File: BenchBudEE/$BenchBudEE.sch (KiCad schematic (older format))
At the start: 0 parts

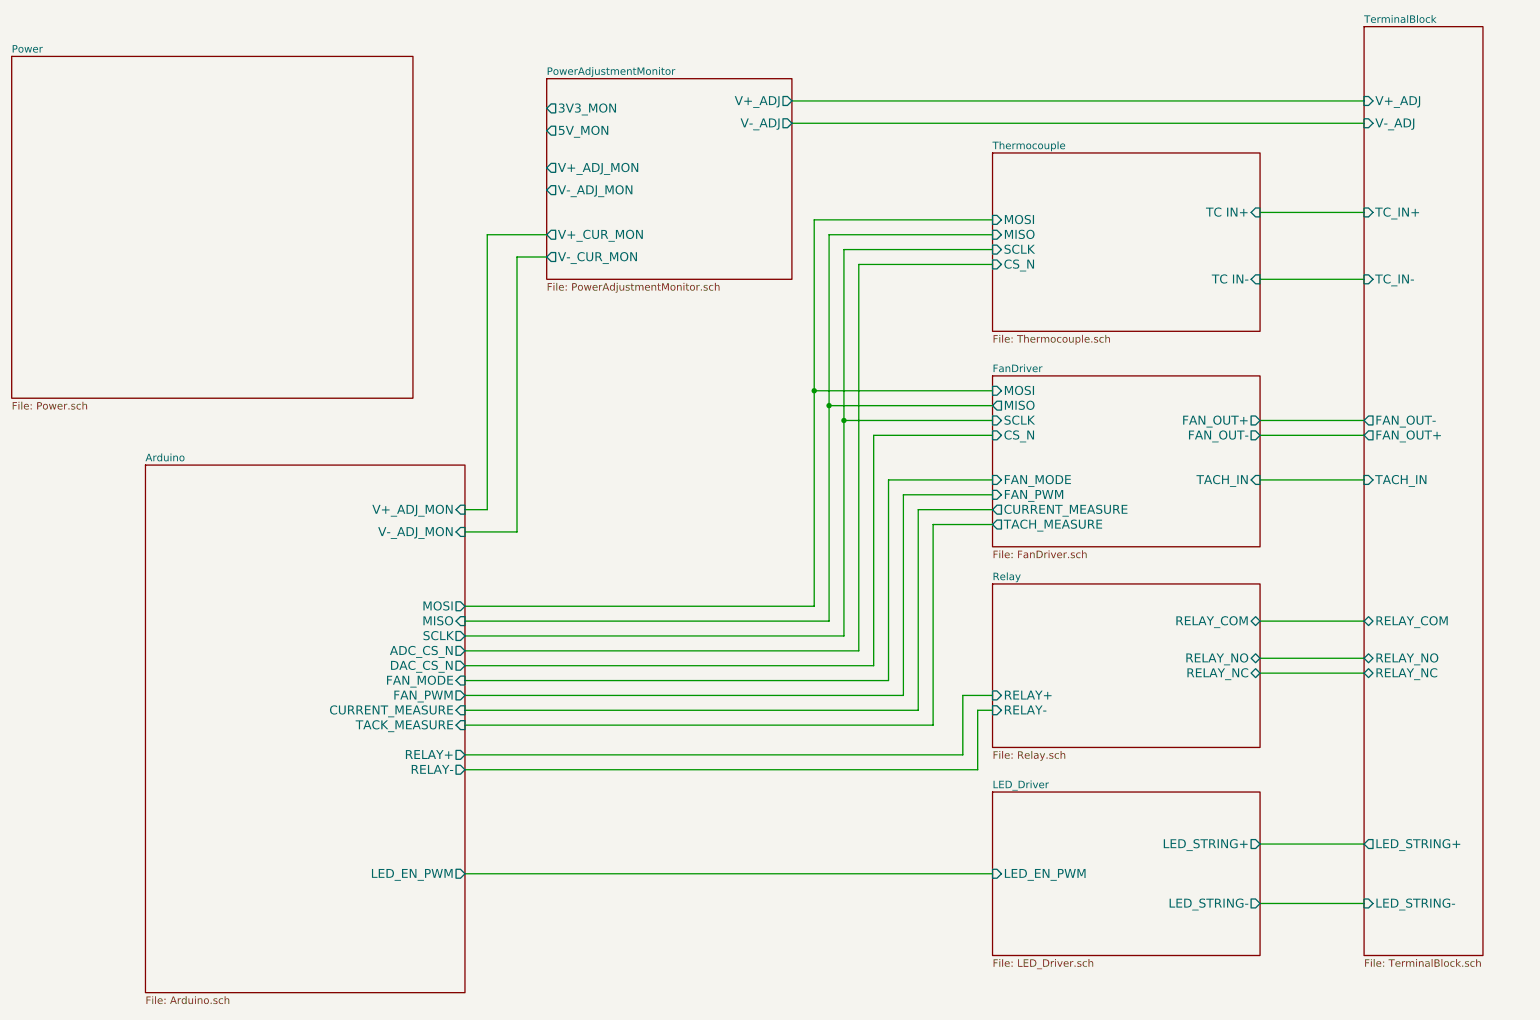
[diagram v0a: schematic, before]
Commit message: Parts added to thermocouple module. Relay & thermocouple rough placement.
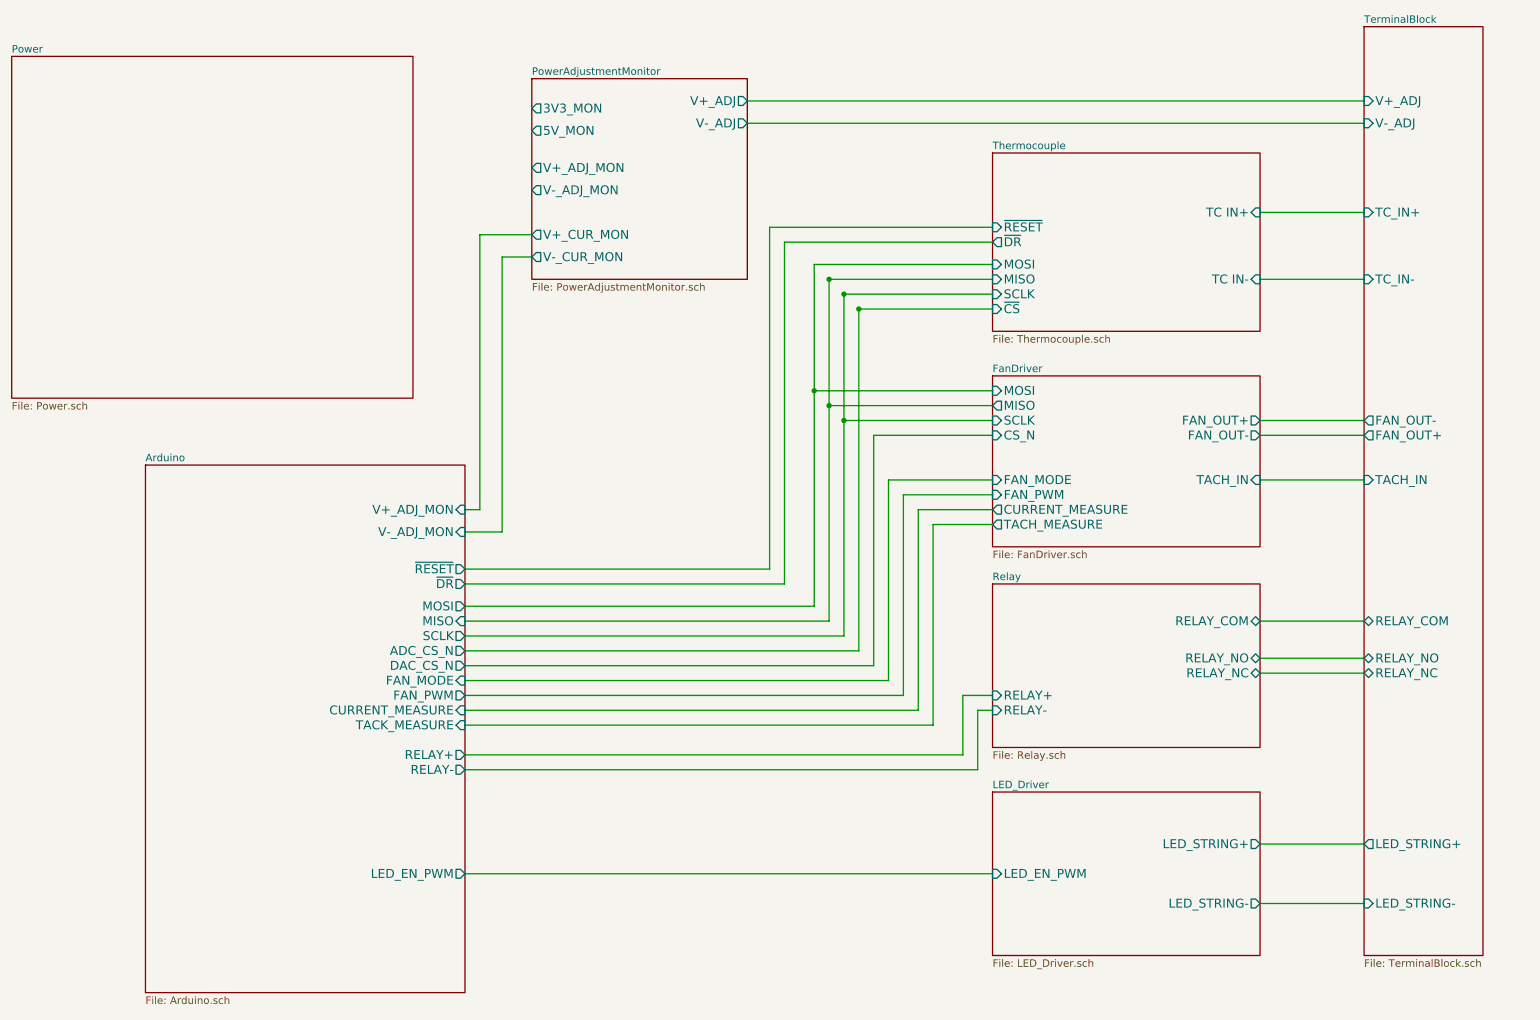
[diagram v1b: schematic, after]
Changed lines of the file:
@@
 Sheet 1 9
 Title ""
-Date "20 feb 2014"
+Date "21 feb 2014"
 Rev ""
 Comp ""
@@
 F2 "TC IN+" I R 9250 1900 60
 F3 "TC IN-" I R 9250 2350 60
-F4 "MISO" I L 7450 2050 60
-F5 "MOSI" I L 7450 1950 60
-F6 "SCLK" I L 7450 2150 60
-F7 "CS_N" I L 7450 2250 60
-$EndSheet
-$Sheet
-S 4450 1000 1650 1350
+F4 "MISO" I L 7450 2350 60
+F5 "MOSI" I L 7450 2250 60
+F6 "SCLK" I L 7450 2450 60
+F7 "~CS" I L 7450 2550 60
+F8 "~DR" O L 7450 2100 60
+F9 "~RESET" I L 7450 2000 60
+$EndSheet
+$Sheet
+S 4350 1000 1450 1350
 U 52F2C572
 F0 "PowerAdjustmentMonitor" 50
 F1 "PowerAdjustmentMonitor.sch" 50
-F2 "V+_ADJ" O R 6100 1150 60
-F3 "V-_ADJ" O R 6100 1300 60
-F4 "3V3_MON" O L 4450 1200 60
-F5 "5V_MON" O L 4450 1350 60
-F6 "V+_ADJ_MON" O L 4450 1600 60
-F7 "V-_ADJ_MON" O L 4450 1750 60
-F8 "V+_CUR_MON" O L 4450 2050 60
-F9 "V-_CUR_MON" O L 4450 2200 60
-$EndSheet
-Wire Wire Line
-	6100 1300 9950 1300
-Wire Wire Line
-	6100 1150 9950 1150
-Wire Wire Line
-	9250 3300 9950 3300
-Wire Wire Line
-	9950 3400 9250 3400
-Wire Wire Line
-	9250 3700 9950 3700
-Wire Wire Line
-	9250 2350 9950 2350
-Wire Wire Line
-	9950 1900 9250 1900
-Wire Wire Line
-	9250 5000 9950 5000
-Wire Wire Line
-	9950 4900 9250 4900
-Wire Wire Line
-	9250 4650 9950 4650
-Wire Wire Line
-	9250 6150 9950 6150
-Wire Wire Line
-	9250 6550 9950 6550
-Wire Wire Line
-	3900 3900 4050 3900
-Wire Wire Line
-	4050 3900 4050 2050
-Wire Wire Line
-	4050 2050 4450 2050
-Wire Wire Line
-	4450 2200 4250 2200
-Wire Wire Line
-	4250 2200 4250 4050
-Wire Wire Line
-	4250 4050 3900 4050
-Wire Wire Line
-	6250 1950 6250 4550
-Wire Wire Line
-	6250 1950 7450 1950
-Wire Wire Line
-	6350 2050 6350 4650
-Wire Wire Line
-	6450 2150 6450 4750
-Wire Wire Line
-	6550 2250 6550 4850
-Wire Wire Line
-	7450 3100 6250 3100
-Connection ~ 6250 3100
-Wire Wire Line
-	7450 3200 6350 3200
-Connection ~ 6350 3200
-Wire Wire Line
-	7450 3300 6450 3300
-Connection ~ 6450 3300
-Wire Wire Line
-	6950 5250 6950 3900
-Wire Wire Line
-	6950 3900 7450 3900
-Wire Wire Line
-	7450 4000 7050 4000
-Wire Wire Line
-	7050 4000 7050 5350
-Wire Wire Line
-	7450 3400 6650 3400
-Wire Wire Line
-	6650 3400 6650 4950
-Wire Wire Line
-	6550 4850 3900 4850
-Wire Wire Line
-	6650 4950 3900 4950
-Wire Wire Line
-	6250 4550 3900 4550
-Wire Wire Line
-	7450 2050 6350 2050
-Wire Wire Line
-	6450 2150 7450 2150
-Wire Wire Line
-	7450 2250 6550 2250
-Wire Wire Line
-	6350 4650 3900 4650
-Wire Wire Line
-	6450 4750 3900 4750
-Wire Wire Line
-	7450 3800 6850 3800
-Wire Wire Line
-	6850 3800 6850 5150
-Wire Wire Line
-	6850 5150 3900 5150
-Wire Wire Line
-	6950 5250 3900 5250
-Wire Wire Line
-	7050 5350 3900 5350
+F2 "V+_ADJ" O R 5800 1150 60
+F3 "V-_ADJ" O R 5800 1300 60
+F4 "3V3_MON" O L 4350 1200 60
+F5 "5V_MON" O L 4350 1350 60
+F6 "V+_ADJ_MON" O L 4350 1600 60
+F7 "V-_ADJ_MON" O L 4350 1750 60
+F8 "V+_CUR_MON" O L 4350 2050 60
+F9 "V-_CUR_MON" O L 4350 2200 60
+$EndSheet
 $Sheet
 S 1750 3600 2150 3550
@@
 F14 "FAN_PWM" O R 3900 5150 60
 F15 "FAN_MODE" I R 3900 5050 60
-$EndSheet
+F16 "~DR" O R 3900 4400 60
+F17 "~RESET" O R 3900 4300 60
+$EndSheet
+Wire Wire Line
+	6750 3700 7450 3700
+Wire Wire Line
+	6750 5050 6750 3700
+Wire Wire Line
+	3900 5050 6750 5050
+Wire Wire Line
+	3900 6350 7450 6350
+Wire Wire Line
+	7350 5650 3900 5650
+Wire Wire Line
+	7350 5250 7350 5650
+Wire Wire Line
+	7450 5250 7350 5250
+Wire Wire Line
+	7250 5150 7450 5150
+Wire Wire Line
+	7250 5550 7250 5150
 Wire Wire Line
 	3900 5550 7250 5550
 Wire Wire Line
-	7250 5550 7250 5150
-Wire Wire Line
-	7250 5150 7450 5150
-Wire Wire Line
-	7450 5250 7350 5250
-Wire Wire Line
-	7350 5250 7350 5650
-Wire Wire Line
-	7350 5650 3900 5650
-Wire Wire Line
-	3900 6350 7450 6350
-Wire Wire Line
-	3900 5050 6750 5050
-Wire Wire Line
-	6750 5050 6750 3700
-Wire Wire Line
-	6750 3700 7450 3700
+	7050 5350 3900 5350
+Wire Wire Line
+	6950 5250 3900 5250
+Wire Wire Line
+	6850 5150 3900 5150
+Wire Wire Line
+	6850 3800 6850 5150
+Wire Wire Line
+	7450 3800 6850 3800
+Wire Wire Line
+	6450 4750 3900 4750
+Wire Wire Line
+	6350 4650 3900 4650
+Wire Wire Line
+	6250 4550 3900 4550
+Wire Wire Line
+	6650 4950 3900 4950
+Wire Wire Line
+	6550 4850 3900 4850
+Wire Wire Line
+	6650 3400 6650 4950
+Wire Wire Line
+	7450 3400 6650 3400
+Wire Wire Line
+	7050 4000 7050 5350
+Wire Wire Line
+	7450 4000 7050 4000
+Wire Wire Line
+	6950 3900 7450 3900
+Wire Wire Line
+	6950 5250 6950 3900
+Connection ~ 6450 3300
+Wire Wire Line
+	7450 3300 6450 3300
+Connection ~ 6350 3200
+Wire Wire Line
+	7450 3200 6350 3200
+Connection ~ 6250 3100
+Wire Wire Line
+	7450 3100 6250 3100
+Wire Wire Line
+	6250 2250 6250 4550
+Wire Wire Line
+	4150 4050 3900 4050
+Wire Wire Line
+	4150 2200 4150 4050
+Wire Wire Line
+	4350 2200 4150 2200
+Wire Wire Line
+	4000 2050 4350 2050
+Wire Wire Line
+	4000 3900 4000 2050
+Wire Wire Line
+	3900 3900 4000 3900
+Wire Wire Line
+	9250 6550 9950 6550
+Wire Wire Line
+	9250 6150 9950 6150
+Wire Wire Line
+	9250 4650 9950 4650
+Wire Wire Line
+	9950 4900 9250 4900
+Wire Wire Line
+	9250 5000 9950 5000
+Wire Wire Line
+	9950 1900 9250 1900
+Wire Wire Line
+	9250 2350 9950 2350
+Wire Wire Line
+	9250 3700 9950 3700
+Wire Wire Line
+	9950 3400 9250 3400
+Wire Wire Line
+	9250 3300 9950 3300
+Wire Wire Line
+	5800 1150 9950 1150
+Wire Wire Line
+	5800 1300 9950 1300
+Wire Wire Line
+	7450 2550 6550 2550
+Connection ~ 6550 2550
+Wire Wire Line
+	6550 2550 6550 4850
+Wire Wire Line
+	7450 2450 6450 2450
+Connection ~ 6450 2450
+Wire Wire Line
+	6450 2450 6450 4750
+Wire Wire Line
+	7450 2350 6350 2350
+Connection ~ 6350 2350
+Wire Wire Line
+	6350 2350 6350 4650
+Wire Wire Line
+	6250 2250 7450 2250
+Wire Wire Line
+	7450 2100 6050 2100
+Wire Wire Line
+	6050 2100 6050 4400
+Wire Wire Line
+	6050 4400 3900 4400
+Wire Wire Line
+	3900 4300 5950 4300
+Wire Wire Line
+	5950 4300 5950 2000
+Wire Wire Line
+	5950 2000 7450 2000
 $EndSCHEMATC
